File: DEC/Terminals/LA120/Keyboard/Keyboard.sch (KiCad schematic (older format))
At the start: 2 parts, among them J1 TO MOTHERBOARD, J2 TO KEYPAD

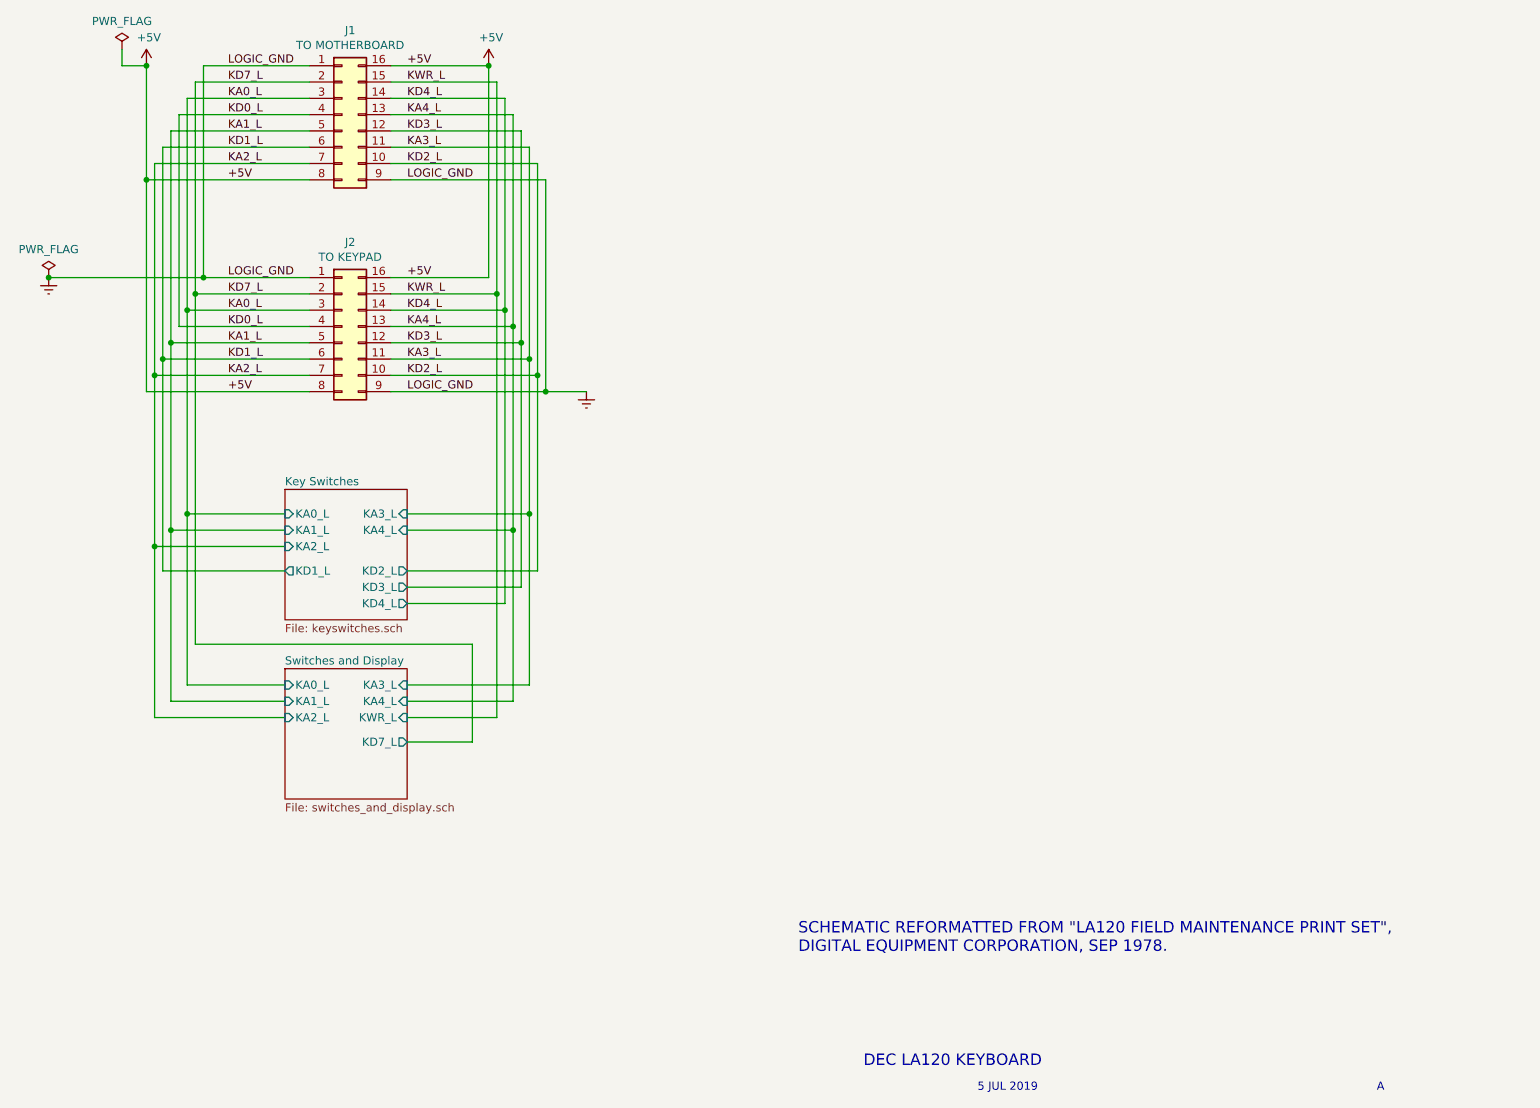
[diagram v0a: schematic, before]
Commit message: Adds DEC LA120 keyboard, keypad, motherboard
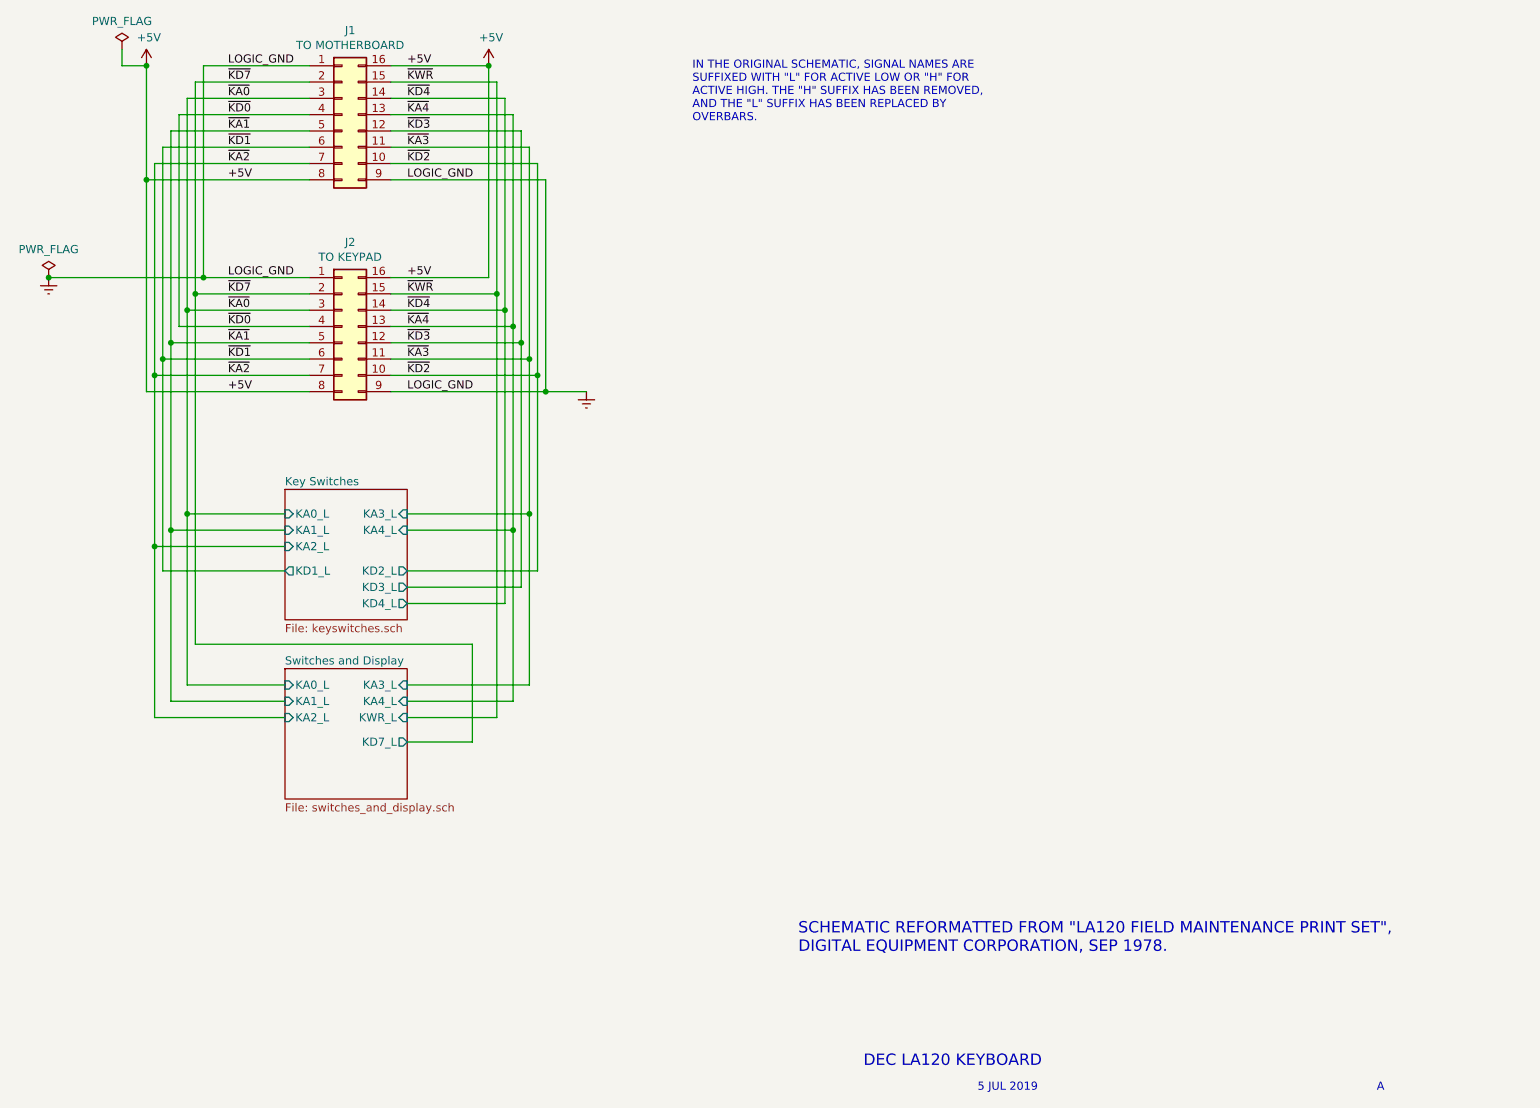
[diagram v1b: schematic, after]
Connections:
- net KA0_L renamed ~KA0
- net KA1_L renamed ~KA1
- net KA2_L renamed ~KA2
- net KA3_L renamed ~KA3
- net KA4_L renamed ~KA4
- net KD0_L renamed ~KD0
- net KD1_L renamed ~KD1
- net KD2_L renamed ~KD2
- net KD3_L renamed ~KD3
- net KD4_L renamed ~KD4
- net KD7_L renamed ~KD7
- net KWR_L renamed ~KWR
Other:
- note added: "IN THE ORIGINAL SCHEMATIC, SIGNAL NAMES ARE\nSUFFIXED WITH "L" FOR ACTIVE LOW OR "H" FOR\nACTIVE HIGH. THE "H" SUFFIX HAS BEEN REMOVED,\nAND THE "L" SUFFIX HAS BEEN REPLACED BY\nOVERBARS."
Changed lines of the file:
@@
 Connection ~ 5500 3350
 Wire Wire Line
-	5500 2050 5500 3350
-Connection ~ 5450 3250
-Wire Wire Line
-	5450 1950 5450 3250
-Connection ~ 5400 3150
-Wire Wire Line
-	5400 1850 5400 3150
-Connection ~ 5350 3050
-Wire Wire Line
-	5350 1750 5350 3050
-Connection ~ 5300 2950
-Wire Wire Line
-	5300 1650 5300 2950
-Connection ~ 5250 2850
-Wire Wire Line
-	5250 1550 5250 2850
-Connection ~ 5200 2750
-Wire Wire Line
-	5200 1450 5200 2750
-Wire Wire Line
-	4550 2850 5250 2850
-Wire Wire Line
-	4550 3050 5350 3050
-Wire Wire Line
-	4550 3250 5450 3250
-Wire Wire Line
-	4550 2950 5300 2950
-Wire Wire Line
-	4550 3150 5400 3150
-Wire Wire Line
 	4550 3350 5500 3350
 Wire Wire Line
 	5150 1350 5150 2650
 Wire Wire Line
-	4550 2750 5200 2750
-Wire Wire Line
 	4550 2650 5150 2650
 Wire Wire Line
@@
 	3050 2050 3050 3350
 Wire Wire Line
-	3100 3250 4050 3250
-Connection ~ 3100 3250
-Wire Wire Line
 	3100 1950 4050 1950
 Wire Wire Line
-	3100 1950 3100 3250
-Wire Wire Line
-	3150 3150 4050 3150
-Connection ~ 3150 3150
-Wire Wire Line
 	3150 1850 4050 1850
 Wire Wire Line
-	3150 1850 3150 3150
-Wire Wire Line
-	3200 3050 4050 3050
-Connection ~ 3200 3050
-Wire Wire Line
 	3200 1750 4050 1750
 Wire Wire Line
-	3200 1750 3200 3050
-Wire Wire Line
-	3250 2950 4050 2950
-Wire Wire Line
 	3250 1650 4050 1650
 Wire Wire Line
 	3250 1650 3250 2950
 Wire Wire Line
-	3300 2850 4050 2850
-Connection ~ 3300 2850
-Wire Wire Line
 	3300 1550 4050 1550
 Wire Wire Line
-	3300 1550 3300 2850
-Wire Wire Line
-	3350 2750 4050 2750
-Connection ~ 3350 2750
-Wire Wire Line
 	3350 1450 4050 1450
-Wire Wire Line
-	3350 1450 3350 2750
 Wire Wire Line
 	3400 2650 4050 2650
@@
 Wire Wire Line
 	3400 1350 3400 2650
-Text Label 4650 2750 0    50   ~ 0
-KWR_L
-Text Label 4650 2850 0    50   ~ 0
-KD4_L
-Text Label 4650 3050 0    50   ~ 0
-KD3_L
-Text Label 4650 3250 0    50   ~ 0
-KD2_L
-Text Label 3550 3150 0    50   ~ 0
-KD1_L
-Text Label 3550 2950 0    50   ~ 0
-KD0_L
-Text Label 3550 2750 0    50   ~ 0
-KD7_L
-Text Label 4650 2950 0    50   ~ 0
-KA4_L
-Text Label 4650 3150 0    50   ~ 0
-KA3_L
-Text Label 3550 3250 0    50   ~ 0
-KA2_L
-Text Label 3550 3050 0    50   ~ 0
-KA1_L
-Text Label 3550 2850 0    50   ~ 0
-KA0_L
 Text Label 4650 2650 0    50   ~ 0
 +5V
@@
 $EndComp
 Text Label 4650 1450 0    50   ~ 0
-KWR_L
+~KWR
 Text Label 4650 1550 0    50   ~ 0
-KD4_L
+~KD4
 Text Label 4650 1750 0    50   ~ 0
-KD3_L
+~KD3
 Text Label 4650 1950 0    50   ~ 0
-KD2_L
+~KD2
 Text Label 3550 1850 0    50   ~ 0
-KD1_L
+~KD1
 Text Label 3550 1650 0    50   ~ 0
-KD0_L
+~KD0
 Text Label 3550 1450 0    50   ~ 0
-KD7_L
+~KD7
 Text Label 4650 1650 0    50   ~ 0
-KA4_L
+~KA4
 Text Label 4650 1850 0    50   ~ 0
-KA3_L
+~KA3
 Text Label 3550 1950 0    50   ~ 0
-KA2_L
+~KA2
 Text Label 3550 1750 0    50   ~ 0
-KA1_L
+~KA1
 Text Label 3550 1550 0    50   ~ 0
-KA0_L
+~KA0
 Text Label 4650 1350 0    50   ~ 0
 +5V
@@
 	3900 4100 3300 4100
 Wire Wire Line
-	3300 4100 3300 2850
-Wire Wire Line
 	3900 4200 3200 4200
 Wire Wire Line
-	3200 4200 3200 3050
-Wire Wire Line
 	3900 4300 3100 4300
 Wire Wire Line
-	3100 4300 3100 3250
-Wire Wire Line
 	3900 4450 3150 4450
 Wire Wire Line
-	3150 4450 3150 3150
-Wire Wire Line
 	4650 4100 5400 4100
 Wire Wire Line
-	5400 4100 5400 3150
-Wire Wire Line
 	4650 4200 5300 4200
 Wire Wire Line
-	5300 4200 5300 2950
-Wire Wire Line
 	4650 4450 5450 4450
 Wire Wire Line
-	5450 4450 5450 3250
-Wire Wire Line
-	5350 4550 5350 3050
-Wire Wire Line
 	4650 4550 5350 4550
 Wire Wire Line
 	4650 4650 5250 4650
-Wire Wire Line
-	5250 4650 5250 2850
 $Sheet
 S 3900 5050 750  800
@@
 	3900 5150 3300 5150
 Wire Wire Line
-	3350 2750 3350 4900
-Wire Wire Line
 	3350 4900 5050 4900
 Wire Wire Line
@@
 	5300 5250 4650 5250
 Connection ~ 5300 4200
-Wire Wire Line
-	5200 2750 5200 5350
 Wire Wire Line
 	5200 5350 4650 5350
@@
 Text Notes 10600 7650 0    50   ~ 0
 A
+Text Notes 6400 1700 0    50   ~ 0
+IN THE ORIGINAL SCHEMATIC, SIGNAL NAMES ARE\nSUFFIXED WITH "L" FOR ACTIVE LOW OR "H" FOR\nACTIVE HIGH. THE "H" SUFFIX HAS BEEN REMOVED,\nAND THE "L" SUFFIX HAS BEEN REPLACED BY\nOVERBARS.
+Wire Wire Line
+	3100 1950 3100 3250
+Wire Wire Line
+	3150 1850 3150 3150
+Wire Wire Line
+	3200 1750 3200 3050
+Wire Wire Line
+	3300 1550 3300 2850
+Wire Wire Line
+	3350 1450 3350 2750
+Wire Wire Line
+	3100 3250 4050 3250
+Wire Wire Line
+	3150 3150 4050 3150
+Wire Wire Line
+	3200 3050 4050 3050
+Wire Wire Line
+	3250 2950 4050 2950
+Wire Wire Line
+	3300 2850 4050 2850
+Wire Wire Line
+	3350 2750 4050 2750
+Text Label 3550 3150 0    50   ~ 0
+~KD1
+Text Label 3550 2950 0    50   ~ 0
+~KD0
+Text Label 3550 2750 0    50   ~ 0
+~KD7
+Text Label 3550 3250 0    50   ~ 0
+~KA2
+Text Label 3550 3050 0    50   ~ 0
+~KA1
+Text Label 3550 2850 0    50   ~ 0
+~KA0
+Connection ~ 3100 3250
+Wire Wire Line
+	3100 3250 3100 4300
+Connection ~ 3150 3150
+Wire Wire Line
+	3150 3150 3150 4450
+Connection ~ 3200 3050
+Wire Wire Line
+	3200 3050 3200 4200
+Connection ~ 3300 2850
+Wire Wire Line
+	3300 2850 3300 4100
+Connection ~ 3350 2750
+Wire Wire Line
+	3350 2750 3350 4900
+Wire Wire Line
+	5200 1450 5200 2750
+Wire Wire Line
+	5500 2050 5500 3350
+Wire Wire Line
+	5450 1950 5450 3250
+Wire Wire Line
+	5400 1850 5400 3150
+Wire Wire Line
+	5350 1750 5350 3050
+Wire Wire Line
+	5300 1650 5300 2950
+Wire Wire Line
+	5250 1550 5250 2850
+Wire Wire Line
+	4550 2750 5200 2750
+Wire Wire Line
+	4550 2850 5250 2850
+Wire Wire Line
+	4550 3050 5350 3050
+Wire Wire Line
+	4550 3250 5450 3250
+Wire Wire Line
+	4550 2950 5300 2950
+Wire Wire Line
+	4550 3150 5400 3150
+Text Label 4650 2750 0    50   ~ 0
+~KWR
+Text Label 4650 2850 0    50   ~ 0
+~KD4
+Text Label 4650 3050 0    50   ~ 0
+~KD3
+Text Label 4650 3250 0    50   ~ 0
+~KD2
+Text Label 4650 2950 0    50   ~ 0
+~KA4
+Text Label 4650 3150 0    50   ~ 0
+~KA3
+Connection ~ 5200 2750
+Wire Wire Line
+	5200 2750 5200 5350
+Connection ~ 5250 2850
+Wire Wire Line
+	5250 2850 5250 4650
+Connection ~ 5300 2950
+Wire Wire Line
+	5300 2950 5300 4200
+Connection ~ 5350 3050
+Wire Wire Line
+	5350 3050 5350 4550
+Connection ~ 5400 3150
+Wire Wire Line
+	5400 3150 5400 4100
+Connection ~ 5450 3250
+Wire Wire Line
+	5450 3250 5450 4450
 $EndSCHEMATC
